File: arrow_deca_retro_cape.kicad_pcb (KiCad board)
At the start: 2 copper layers, 97.5 x 65.6 mm, 14 parts

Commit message: updated readme
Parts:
- removed LO3: OSHW-Logo2_14.6x12mm_SilkScreen, Symbol:OSHW-Logo2_14.6x12mm_SilkScreen
- LO1: moved to F.Cu
- moved LO2 111.0 mm to (167.6, 73.0)
- moved LO1 69.9 mm to (127.6, 88.3), turned to 0 degrees
- moved LO4 46.4 mm to (106.7, 113.0)

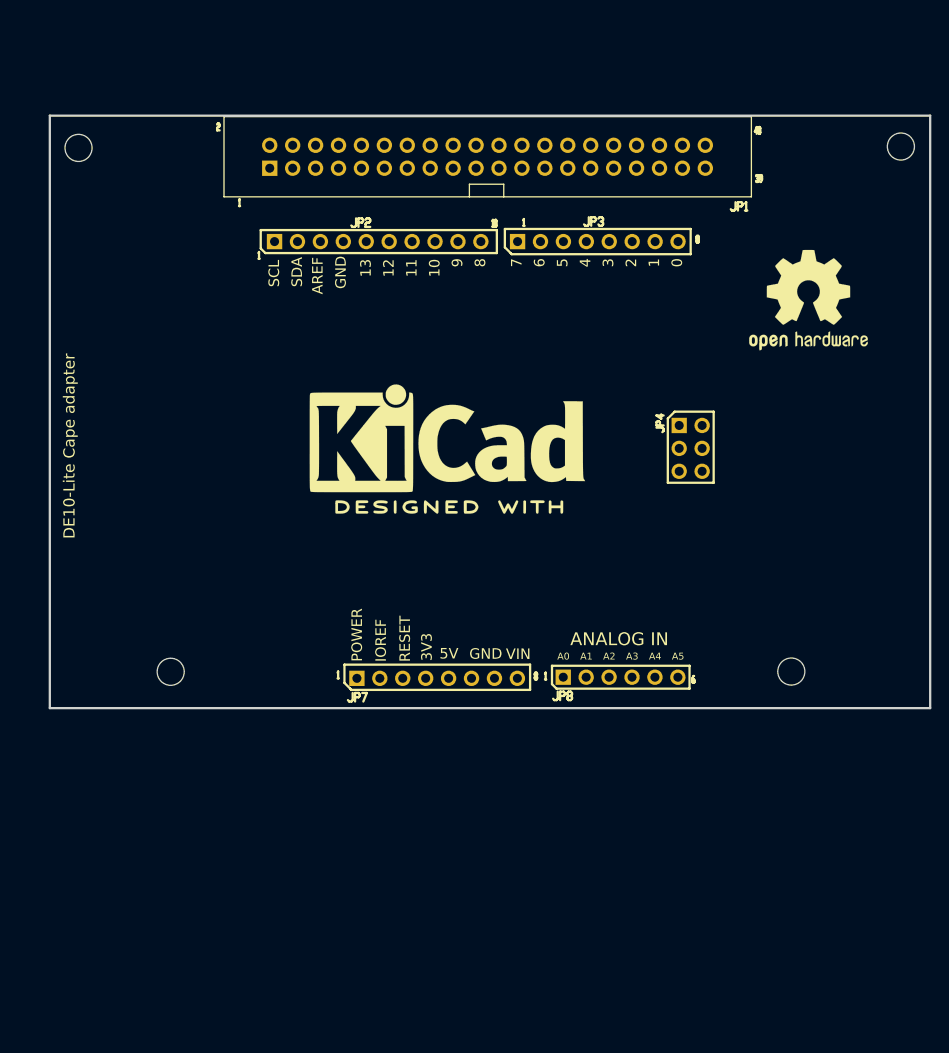
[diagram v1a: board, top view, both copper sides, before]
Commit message: added beaglebone headers
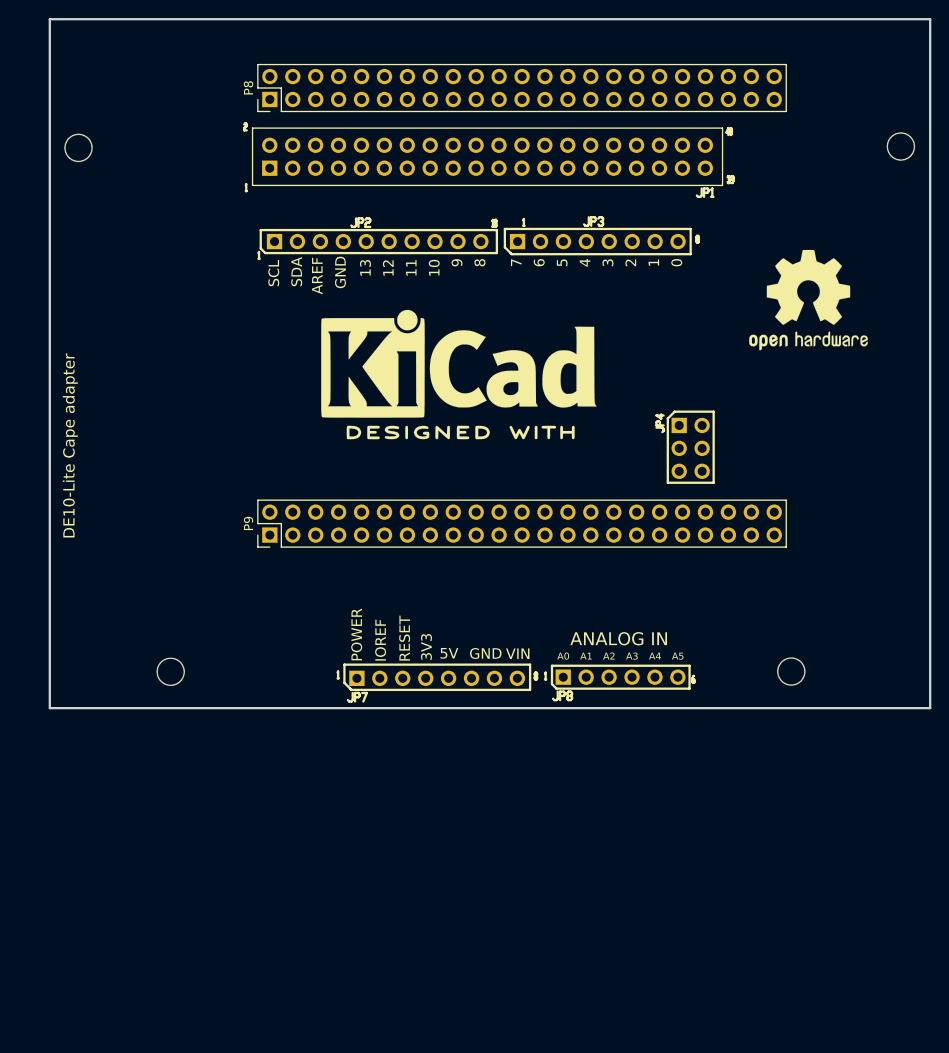
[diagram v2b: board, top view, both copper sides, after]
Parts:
- added P8: BeagleBone_Black_Header, Connector_PinHeader_2.54mm:PinHeader_2x23_P2.54mm_Vertical, F.Cu at (108.0, 50.8)
- added P9: BeagleBone_Black_Header, Connector_PinHeader_2.54mm:PinHeader_2x23_P2.54mm_Vertical, F.Cu at (108.0, 99.1)
- moved LO1 8.35 mm to (128.9, 80.0)
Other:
- board size 97.5 x 65.6 mm -> 97.5 x 76.3 mm
